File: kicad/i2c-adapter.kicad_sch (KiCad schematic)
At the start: 44 parts, among them J1 Conn_02x13_Top_Bottom, J10 AUX IN, J11 +5V, J2 I2C-1, J3 I2C-2, J4 I2C-3, J5 I2C-4, J6 SPI-1, J7 SPI-2, J8 SPI-3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

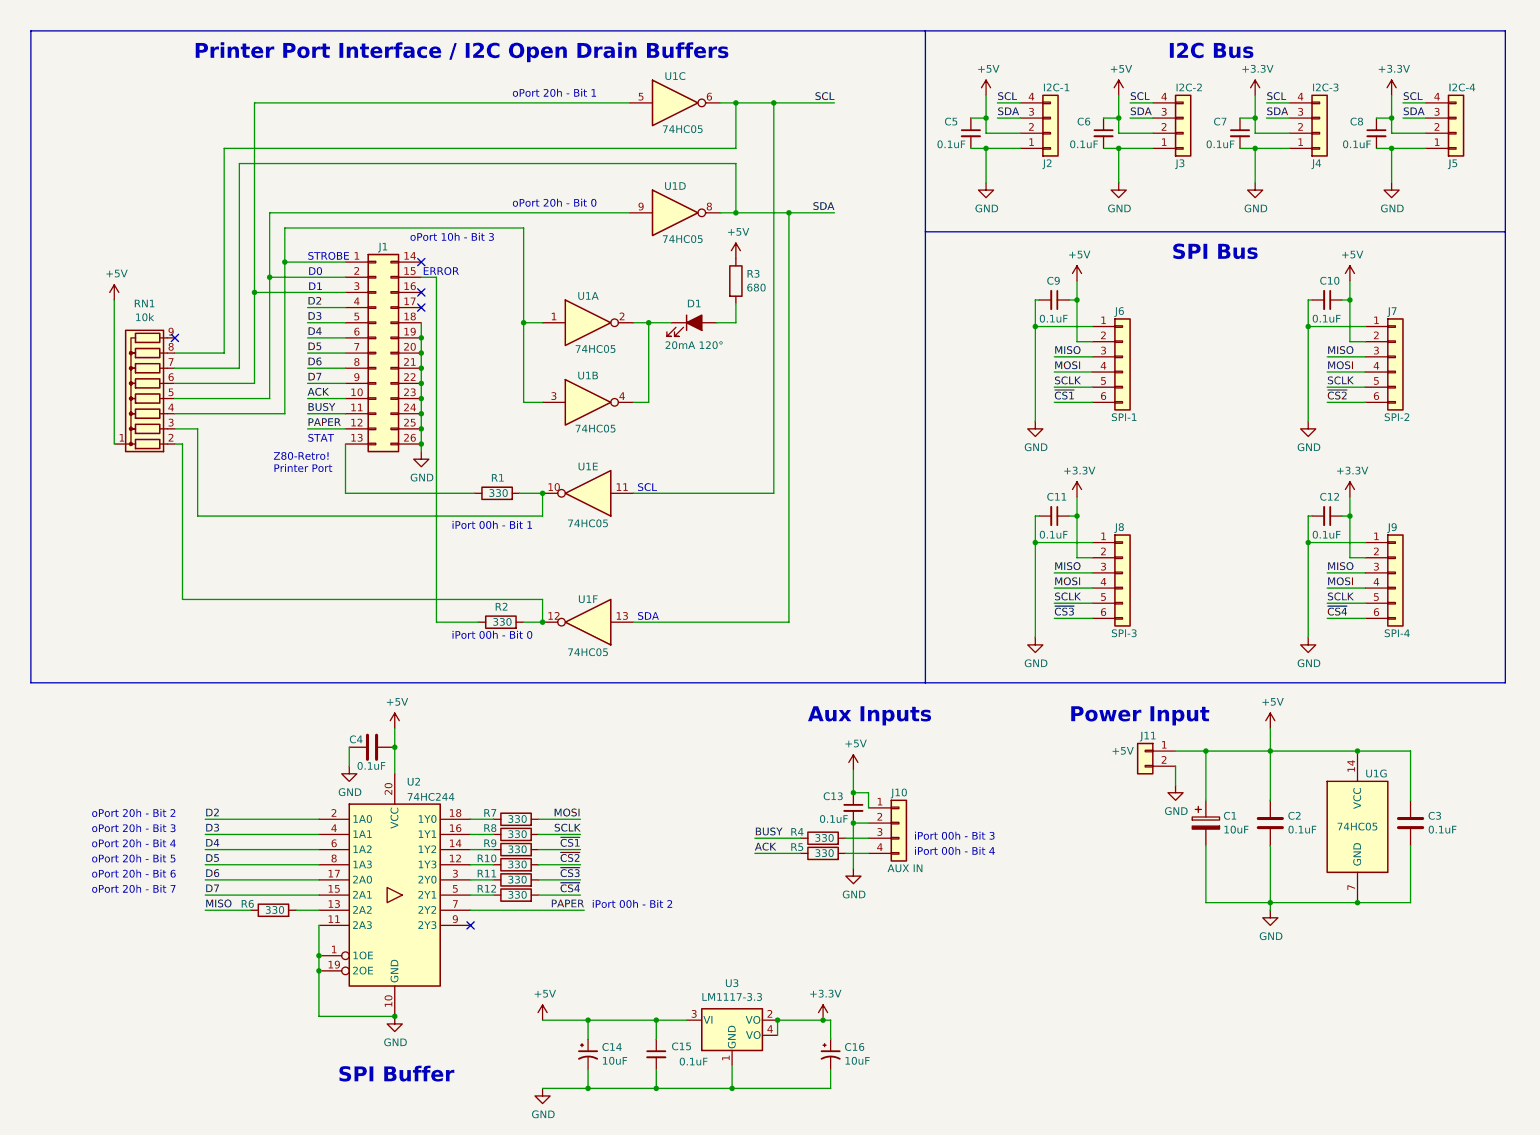
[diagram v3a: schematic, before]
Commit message: Added Adafruit compatible STEMMA QT I2C Connector and EyeSPI connector.
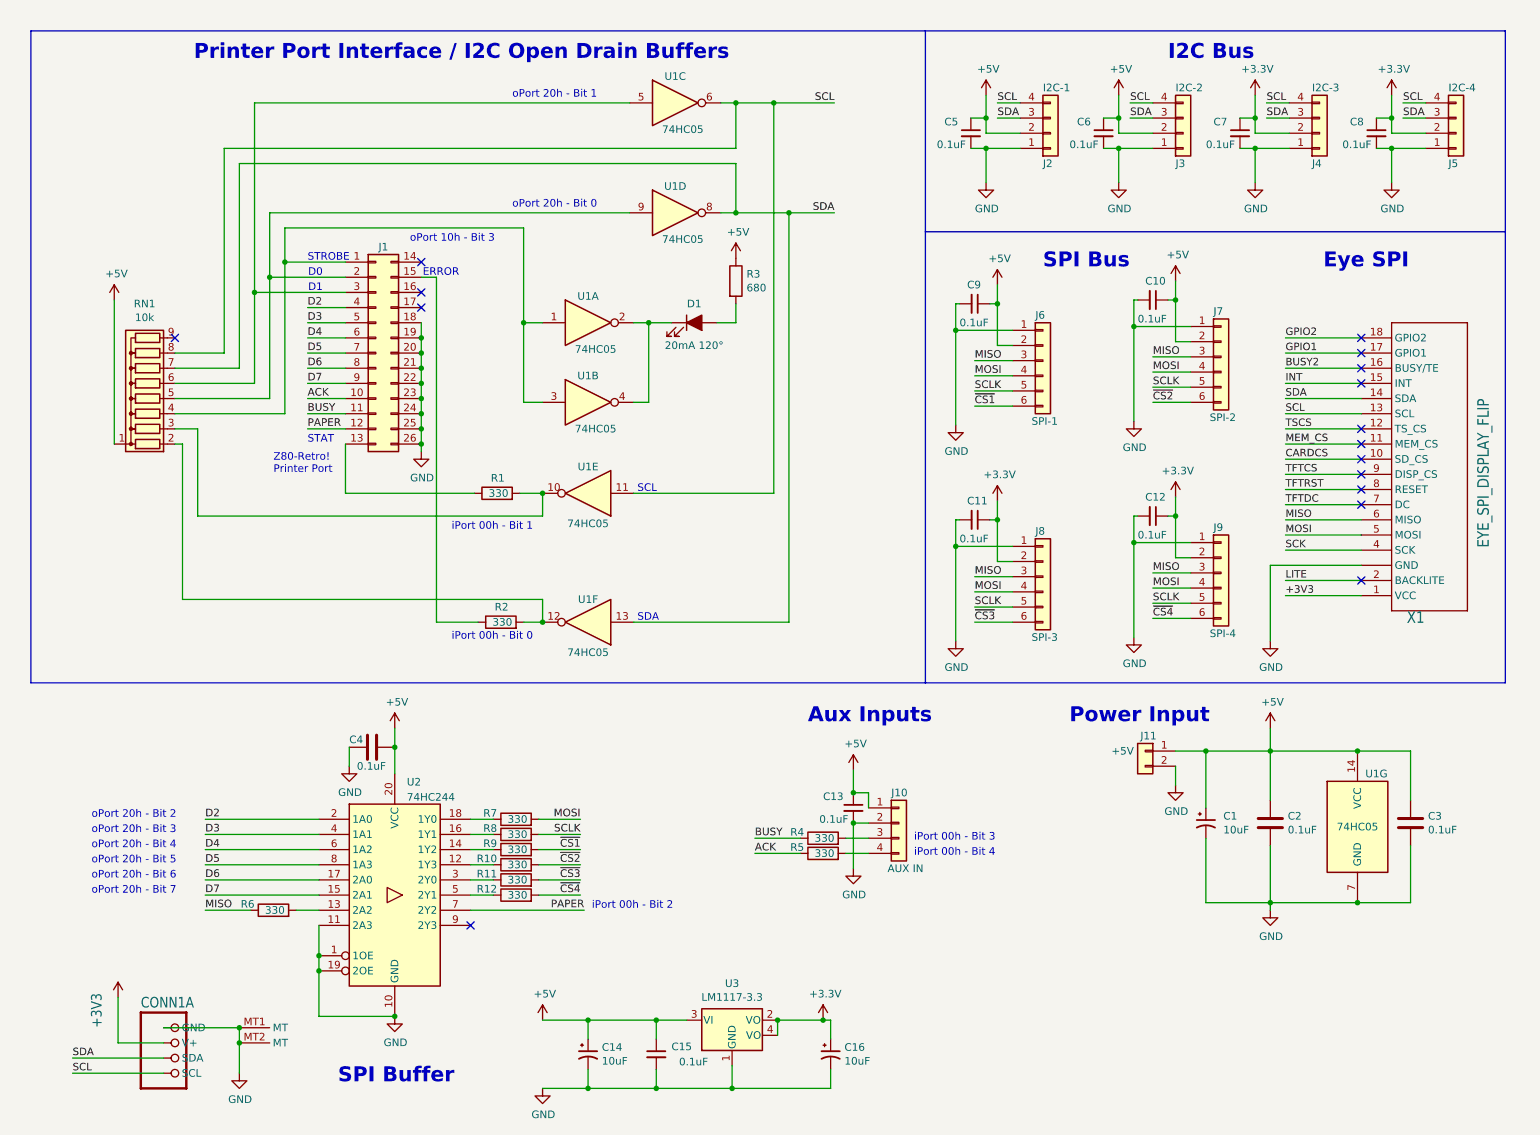
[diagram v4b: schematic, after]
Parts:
- added CONN1: STEMMA_I2C_QT, i2c-adapter:JST_SH4, symbol i2c-adapter:STEMMA_I2C_QT
- added X1: EYE_SPI_DISPLAY_FLIP, i2c-adapter:EYE_SPI_DISPLAY_BOTCONTACT, symbol Adafruit EYESPI Breakout Board-eagle-import:EYE_SPI_DISPLAY_FLIP
- C1: symbol Device:C_Polarized -> Device:C_Polarized_Small_US; LCSC (none) -> C15850
- C10, C11, C12, C13, C15, C2, C3, C4, C5, C6, C7, C8, C9: LCSC (none) -> C28233
- C14, C16: symbol 2063-Z80-rescue:CP1_Small-Device -> Device:C_Polarized_Small_US; LCSC (none) -> C15850
- D1: LCSC (none) -> C375546
- J1: footprint Connector_PinSocket_2.54mm:PinSocket_2x13_P2.54mm_Vertical -> i2c-adapter:PinSocket_2x13_P2.54mm_Vertical
- R1, R10, R11, R12, R2, R4, R5, R6, R7, R8, R9: LCSC (none) -> C17630
- R3: LCSC (none) -> C17798
- U3: footprint digikey-footprints:SOT-223 -> i2c-adapter:SOT-223; symbol 2063-Z80-rescue:LM1117-3.3-jb-symbol -> i2c-adapter:LM1117-3.3; LCSC (none) -> C26537
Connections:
- net +3V3: now also CONN1.2 (V+), X1.1 (VCC)
- net GND: now also CONN1.1 (GND), CONN1.MT1 (MT), CONN1.MT2 (MT), X1.3 (GND), X1.SUPPORT1 (GND), X1.SUPPORT2 (GND)
- net MISO: now also X1.6 (MISO)
- net MOSI: now also X1.5 (MOSI)
- net SCL: now also CONN1.4 (SCL), X1.13 (SCL)
- net SDA: now also CONN1.3 (SDA), X1.14 (SDA)
- new net BUSY2: X1.16 (BUSY/TE)
- new net CARDCS: X1.10 (SD_CS)
- new net GPIO1: X1.17 (GPIO1)
- new net GPIO2: X1.18 (GPIO2)
- new net INT: X1.15 (INT)
- new net LITE: X1.2 (BACKLITE)
- new net MEM_CS: X1.11 (MEM_CS)
- new net SCK: X1.4 (SCK)
- new net TFTCS: X1.9 (DISP_CS)
- new net TFTDC: X1.7 (DC)
- new net TFTRST: X1.8 (RESET)
- new net TSCS: X1.12 (TS_CS)
- no-connect marks 5 -> 16
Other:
- note added: "Eye SPI"
- moved on the sheet: C10, C11, C12, C9, J6, J7, J8, J9

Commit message: Finish up cleanup of both Schematic and PCB; Give Adafruit connectors labels.
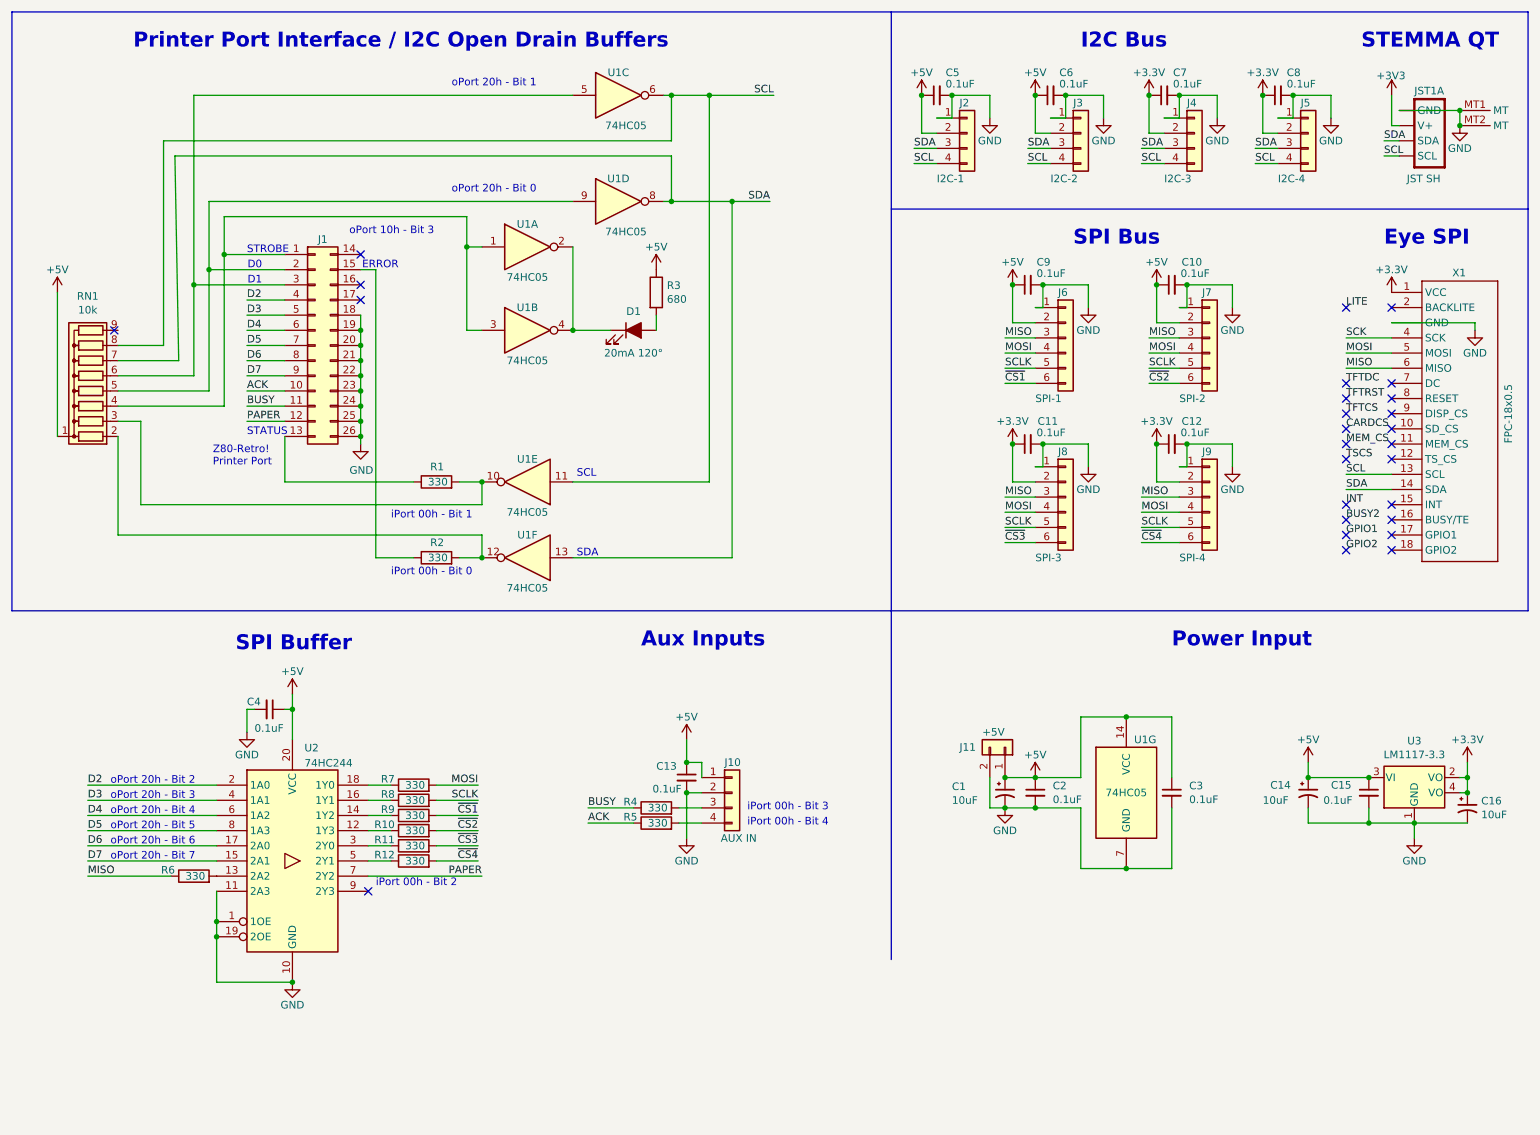
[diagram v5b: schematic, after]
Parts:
- C2, C3, C4: symbol Device:C -> Device:C_Small
- JST1: renamed from CONN1; value STEMMA_I2C_QT -> JST SH
- X1: value EYE_SPI_DISPLAY_FLIP -> FPC-18x0.5
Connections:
- net BUSY2: no longer X1.16 (BUSY/TE)
- net CARDCS: no longer X1.10 (SD_CS)
- net GPIO1: no longer X1.17 (GPIO1)
- net GPIO2: no longer X1.18 (GPIO2)
- net INT: no longer X1.15 (INT)
- net LITE: no longer X1.2 (BACKLITE)
- net MEM_CS: no longer X1.11 (MEM_CS)
- net TFTCS: no longer X1.9 (DISP_CS)
- net TFTDC: no longer X1.7 (DC)
- net TFTRST: no longer X1.8 (RESET)
- net TSCS: no longer X1.12 (TS_CS)
- no-connect marks 16 -> 27
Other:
- note added: "STATUS"
- note added: "STEMMA QT"
- note removed: "STAT"
- moved on the sheet: C1, C10, C11, C12, C13, C14, C15, C16, C2, C3, C4, C5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

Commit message: Make the Adafruit connectors easier to understand; Label sockets with Chip Part #
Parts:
- renumbered X1 to EyeSPI1, JST1 to StemmaQT1
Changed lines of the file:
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@@
   (symbol (lib_id "i2c-adapter:STEMMA_I2C_QT") (at 255.27 29.21 0) (unit 2)
     (in_bom yes) (on_board yes)
-    (property "Reference" "JST1" (id 0) (at 251.46 20.955 0)
+    (property "Reference" "StemmaQT1" (id 0) (at 251.46 20.955 0)
       (effects (font (size 1.778 1.5113)) (justify left bottom) hide)
     )
@@
   (symbol (lib_id "Adafruit EYESPI Breakout Board-eagle-import:EYE_SPI_DISPLAY_FLIP") (at 248.92 80.01 0) (unit 1)
     (in_bom yes) (on_board yes)
-    (property "Reference" "X1" (id 0) (at 254 57.15 0)
+    (property "Reference" "EyeSPI1" (id 0) (at 254 57.15 0)
       (effects (font (size 1.27 1.27)) (justify left bottom))
     )
@@
   (symbol (lib_id "i2c-adapter:STEMMA_I2C_QT") (at 255.27 31.75 0) (unit 3)
     (in_bom yes) (on_board yes)
-    (property "Reference" "JST1" (id 0) (at 251.46 23.495 0)
+    (property "Reference" "StemmaQT1" (id 0) (at 251.46 23.495 0)
       (effects (font (size 1.778 1.5113)) (justify left bottom) hide)
     )
@@
   (symbol (lib_name "STEMMA_I2C_QT_1") (lib_id "i2c-adapter:STEMMA_I2C_QT") (at 245.11 34.29 0) (unit 1)
     (in_bom yes) (on_board yes)
-    (property "Reference" "JST1" (id 0) (at 247.65 26.67 0)
+    (property "Reference" "StemmaQT1" (id 0) (at 247.65 26.67 0)
       (effects (font (size 1.27 1.27)) (justify left bottom))
     )
@@
       (reference "D1") (unit 1) (value "20mA 120°") (footprint "LED_SMD:LED_0805_2012Metric_Pad1.15x1.40mm_HandSolder")
     )
+    (path "/5c0d2f8e-f0bd-4cf5-8873-87b92fe3ef7e"
+      (reference "EyeSPI1") (unit 1) (value "FPC-18x0.5") (footprint "i2c-adapter:EYE_SPI_DISPLAY_BOTCONTACT")
+    )
     (path "/00000000-0000-0000-0000-00006296f9b4"
       (reference "J1") (unit 1) (value "Conn_02x13_Top_Bottom") (footprint "i2c-adapter:PinSocket_2x13_P2.54mm_Vertical")
@@
       (reference "J11") (unit 1) (value "+5V") (footprint "Connector_PinHeader_2.54mm:PinHeader_1x02_P2.54mm_Vertical")
     )
-    (path "/ab3627a7-7803-4c59-9be1-60b81c365de8"
-      (reference "JST1") (unit 1) (value "JST SH") (footprint "i2c-adapter:JST_SH4")
-    )
-    (path "/4e5b0047-2cdc-403e-853e-5f49d3a58b1a"
-      (reference "JST1") (unit 2) (value "JST SH") (footprint "i2c-adapter:JST_SH4")
-    )
-    (path "/902b9269-6591-46a9-9c36-7921392c16aa"
-      (reference "JST1") (unit 3) (value "JST SH") (footprint "i2c-adapter:JST_SH4")
-    )
     (path "/00000000-0000-0000-0000-000062a302fd"
       (reference "R1") (unit 1) (value "330") (footprint "Resistor_SMD:R_0805_2012Metric_Pad1.20x1.40mm_HandSolder")
@@
       (reference "RN1") (unit 1) (value "10k") (footprint "Resistor_THT:R_Array_SIP9")
     )
+    (path "/ab3627a7-7803-4c59-9be1-60b81c365de8"
+      (reference "StemmaQT1") (unit 1) (value "JST SH") (footprint "i2c-adapter:JST_SH4")
+    )
+    (path "/4e5b0047-2cdc-403e-853e-5f49d3a58b1a"
+      (reference "StemmaQT1") (unit 2) (value "JST SH") (footprint "i2c-adapter:JST_SH4")
+    )
+    (path "/902b9269-6591-46a9-9c36-7921392c16aa"
+      (reference "StemmaQT1") (unit 3) (value "JST SH") (footprint "i2c-adapter:JST_SH4")
+    )
     (path "/00000000-0000-0000-0000-00006296e541"
       (reference "U1") (unit 1) (value "74HC05") (footprint "Package_DIP:DIP-14_W7.62mm_Socket")
@@
       (reference "U3") (unit 1) (value "LM1117-3.3") (footprint "i2c-adapter:SOT-223")
     )
-    (path "/5c0d2f8e-f0bd-4cf5-8873-87b92fe3ef7e"
-      (reference "X1") (unit 1) (value "FPC-18x0.5") (footprint "i2c-adapter:EYE_SPI_DISPLAY_BOTCONTACT")
-    )
-  )
+  )
